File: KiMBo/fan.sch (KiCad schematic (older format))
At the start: 36 parts

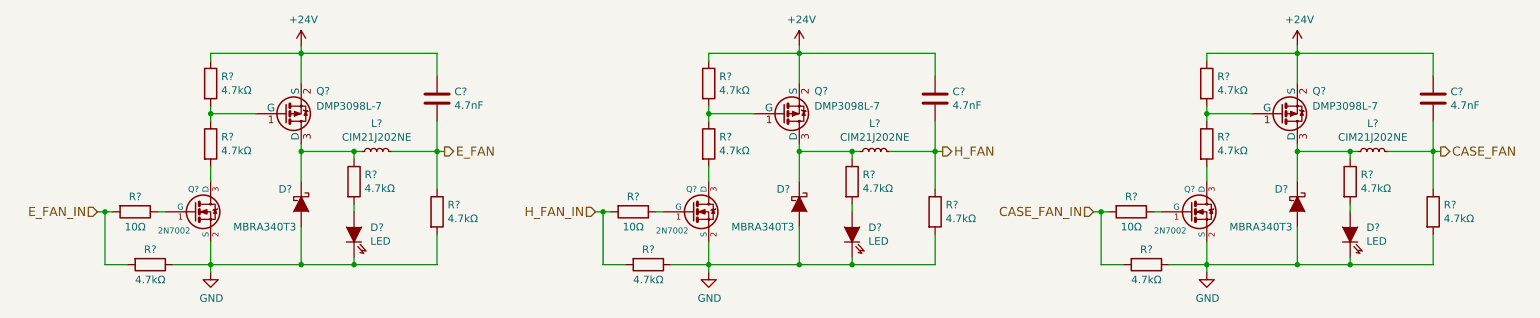
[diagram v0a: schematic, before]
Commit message: Update ferrite values, select fuse based on interrupt rating
The PSU needs to be able to supply at LEAST 25A to blow the fuse
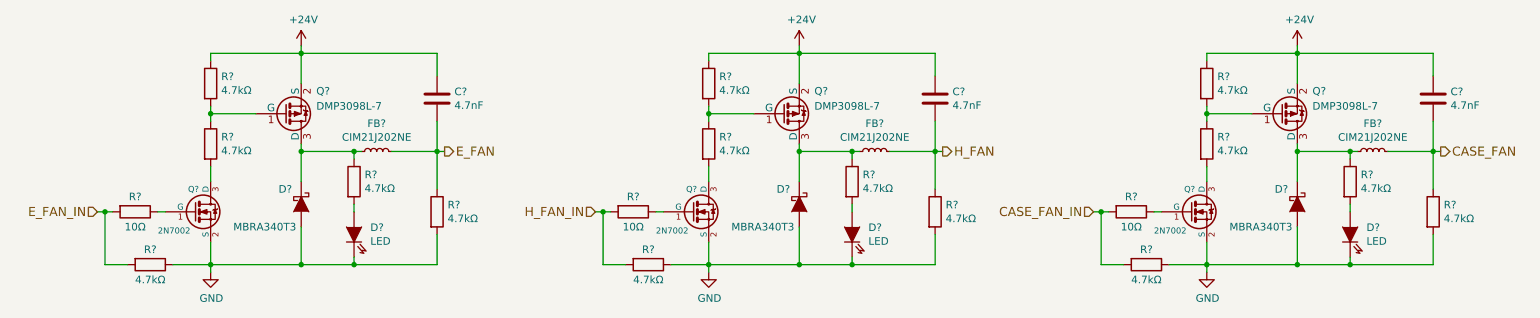
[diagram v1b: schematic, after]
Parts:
- gave numbers to parts that had none: 1
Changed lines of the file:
@@
 $EndComp
 $Comp
-L INDUCTOR_Small L?
+L INDUCTOR_Small FB?
 U 1 1 5B5F15E2
 P 5300 5200
-F 0 "L?" V 5485 5200 50  0000 C CNN
+F 0 "FB?" V 5485 5200 50  0000 C CNN
 F 1 "CIM21J202NE" V 5394 5200 50  0000 C CNN
 F 2 "" H 5300 5200 50  0000 C CNN
@@
 $EndComp
 $Comp
-L INDUCTOR_Small L?
+L INDUCTOR_Small FB?
 U 1 1 5B5F2422
 P 8600 5200
-F 0 "L?" V 8785 5200 50  0000 C CNN
+F 0 "FB?" V 8785 5200 50  0000 C CNN
 F 1 "CIM21J202NE" V 8694 5200 50  0000 C CNN
 F 2 "" H 8600 5200 50  0000 C CNN
@@
 $EndComp
 $Comp
-L INDUCTOR_Small L?
+L INDUCTOR_Small FB?
 U 1 1 5B5F2A0D
 P 11900 5200
-F 0 "L?" V 12085 5200 50  0000 C CNN
+F 0 "FB?" V 12085 5200 50  0000 C CNN
 F 1 "CIM21J202NE" V 11994 5200 50  0000 C CNN
 F 2 "" H 11900 5200 50  0000 C CNN

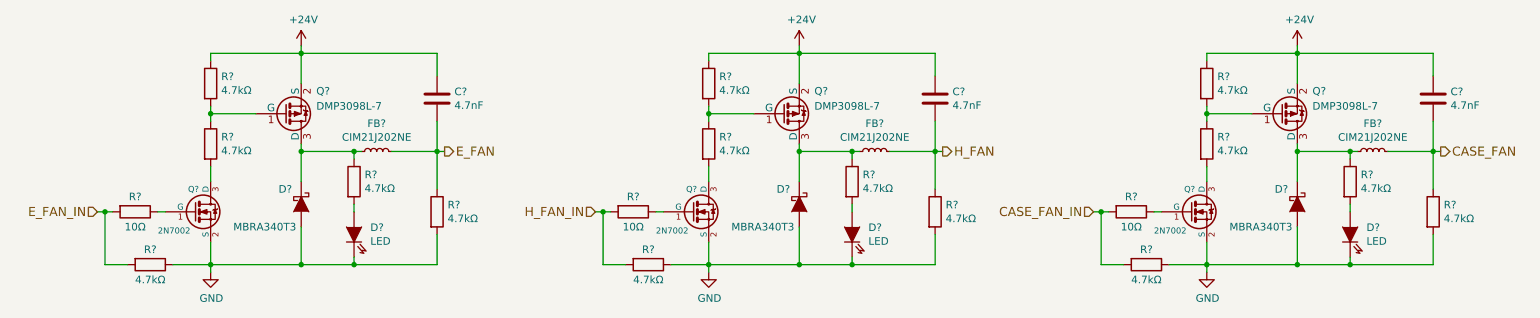
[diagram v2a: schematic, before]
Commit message: Annotate all components, now passing ERC, added ferrites to the rest of the connectors
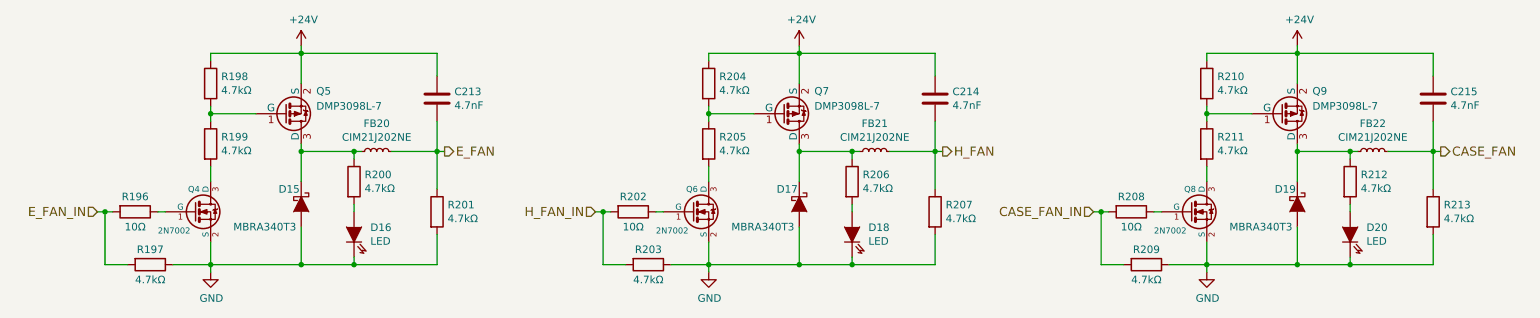
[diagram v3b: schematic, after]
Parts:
- gave numbers to parts that had none: 36
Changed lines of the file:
@@
 E_FAN
 $Comp
-L +24V #PWR0273
+L +24V #PWR0286
 U 1 1 5B5EFE55
 P 4800 4500
-F 0 "#PWR0273" H 4800 4350 50  0001 C CNN
+F 0 "#PWR0286" H 4800 4350 50  0001 C CNN
 F 1 "+24V" H 4815 4673 50  0000 C CNN
 F 2 "" H 4800 4500 50  0000 C CNN
@@
 $EndComp
 $Comp
-L GND #PWR0274
+L GND #PWR0287
 U 1 1 5B5EFE5B
 P 4200 6000
-F 0 "#PWR0274" H 4200 5750 50  0001 C CNN
+F 0 "#PWR0287" H 4200 5750 50  0001 C CNN
 F 1 "GND" H 4205 5827 50  0000 C CNN
 F 2 "" H 4200 6000 50  0000 C CNN
@@
 $EndComp
 $Comp
-L D_Schottky D?
+L D_Schottky D15
 U 1 1 5B5EFE61
 P 4800 5550
-F 0 "D?" V 4700 5400 50  0000 L CNN
+F 0 "D15" V 4700 5400 50  0000 L CNN
 F 1 "MBRA340T3" V 4950 5100 50  0000 L CNN
 F 2 "" H 4800 5550 50  0000 C CNN
@@
 $EndComp
 $Comp
-L R R?
+L R R196
 U 1 1 5B5EFE68
 P 3700 5600
-F 0 "R?" V 3600 5600 50  0000 C CNN
+F 0 "R196" V 3600 5600 50  0000 C CNN
 F 1 "10Ω" V 3800 5600 50  0000 C CNN
 F 2 "" V 3630 5600 50  0000 C CNN
@@
 $EndComp
 $Comp
-L 2N7002P,215 Q?
+L 2N7002P,215 Q4
 U 1 1 5B5EFE6F
 P 4100 5600
-F 0 "Q?" H 4050 5750 40  0000 L CNN
+F 0 "Q4" H 4050 5750 40  0000 L CNN
 F 1 "2N7002" H 3850 5475 40  0000 L CNN
 F 2 "SOT-23" H 3970 5702 29  0001 C CNN
@@
 $EndComp
 $Comp
-L LED_Short D?
+L LED_Short D16
 U 1 1 5B5EFE77
 P 5150 5750
-F 0 "D?" V 5196 5642 50  0000 R CNN
+F 0 "D16" V 5196 5642 50  0000 R CNN
 F 1 "LED" V 5105 5642 50  0000 R CNN
 F 2 "" H 5150 5750 50  0000 C CNN
@@
 $EndComp
 $Comp
-L R R?
+L R R200
 U 1 1 5B5EFE7E
 P 5150 5400
-F 0 "R?" H 5220 5446 50  0000 L CNN
+F 0 "R200" H 5220 5446 50  0000 L CNN
 F 1 "4.7kΩ" H 5220 5355 50  0000 L CNN
 F 2 "" V 5080 5400 50  0000 C CNN
@@
 $EndComp
 $Comp
-L R R?
+L R R198
 U 1 1 5B5EFE85
 P 4200 4750
-F 0 "R?" H 4270 4796 50  0000 L CNN
+F 0 "R198" H 4270 4796 50  0000 L CNN
 F 1 "4.7kΩ" H 4270 4705 50  0000 L CNN
 F 2 "" V 4130 4750 50  0000 C CNN
@@
 $EndComp
 $Comp
-L R R?
+L R R199
 U 1 1 5B5EFE8C
 P 4200 5150
-F 0 "R?" H 4270 5196 50  0000 L CNN
+F 0 "R199" H 4270 5196 50  0000 L CNN
 F 1 "4.7kΩ" H 4270 5105 50  0000 L CNN
 F 2 "" V 4130 5150 50  0000 C CNN
@@
 $EndComp
 $Comp
-L R R?
+L R R197
 U 1 1 5B5EFE93
 P 3800 5950
-F 0 "R?" V 3700 5950 50  0000 C CNN
+F 0 "R197" V 3700 5950 50  0000 C CNN
 F 1 "4.7kΩ" V 3900 5950 50  0000 C CNN
 F 2 "" V 3730 5950 50  0000 C CNN
@@
 $EndComp
 $Comp
-L R R?
+L R R201
 U 1 1 5B5EFE9A
 P 5700 5600
-F 0 "R?" H 5770 5646 50  0000 L CNN
+F 0 "R201" H 5770 5646 50  0000 L CNN
 F 1 "4.7kΩ" H 5770 5555 50  0000 L CNN
 F 2 "" V 5630 5600 50  0000 C CNN
@@
 $EndComp
 $Comp
-L C C?
+L C C213
 U 1 1 5B5EFEA1
 P 5700 4850
-F 0 "C?" H 5815 4896 50  0000 L CNN
+F 0 "C213" H 5815 4896 50  0000 L CNN
 F 1 "4.7nF" H 5815 4805 50  0000 L CNN
 F 2 "" H 5738 4700 50  0000 C CNN
@@
 	4200 4550 5700 4550
 $Comp
-L DMP3098L-7 Q?
+L DMP3098L-7 Q5
 U 1 1 5B5EFEC7
 P 4700 4950
-F 0 "Q?" H 4900 5100 50  0000 L CNN
+F 0 "Q5" H 4900 5100 50  0000 L CNN
 F 1 "DMP3098L-7" H 4900 5000 50  0000 L CNN
 F 2 "TO_SOT_Packages_SMD:SOT-23" H 4950 5025 50  0001 L CNN
@@
 $EndComp
 $Comp
-L INDUCTOR_Small FB?
+L INDUCTOR_Small FB20
 U 1 1 5B5F15E2
 P 5300 5200
-F 0 "FB?" V 5485 5200 50  0000 C CNN
+F 0 "FB20" V 5485 5200 50  0000 C CNN
 F 1 "CIM21J202NE" V 5394 5200 50  0000 C CNN
 F 2 "" H 5300 5200 50  0000 C CNN
@@
 H_FAN
 $Comp
-L +24V #PWR0275
+L +24V #PWR0288
 U 1 1 5B5F23AA
 P 8100 4500
-F 0 "#PWR0275" H 8100 4350 50  0001 C CNN
+F 0 "#PWR0288" H 8100 4350 50  0001 C CNN
 F 1 "+24V" H 8115 4673 50  0000 C CNN
 F 2 "" H 8100 4500 50  0000 C CNN
@@
 $EndComp
 $Comp
-L GND #PWR0276
+L GND #PWR0289
 U 1 1 5B5F23B0
 P 7500 6000
-F 0 "#PWR0276" H 7500 5750 50  0001 C CNN
+F 0 "#PWR0289" H 7500 5750 50  0001 C CNN
 F 1 "GND" H 7505 5827 50  0000 C CNN
 F 2 "" H 7500 6000 50  0000 C CNN
@@
 $EndComp
 $Comp
-L D_Schottky D?
+L D_Schottky D17
 U 1 1 5B5F23B6
 P 8100 5550
-F 0 "D?" V 8000 5400 50  0000 L CNN
+F 0 "D17" V 8000 5400 50  0000 L CNN
 F 1 "MBRA340T3" V 8250 5100 50  0000 L CNN
 F 2 "" H 8100 5550 50  0000 C CNN
@@
 $EndComp
 $Comp
-L R R?
+L R R202
 U 1 1 5B5F23BD
 P 7000 5600
-F 0 "R?" V 6900 5600 50  0000 C CNN
+F 0 "R202" V 6900 5600 50  0000 C CNN
 F 1 "10Ω" V 7100 5600 50  0000 C CNN
 F 2 "" V 6930 5600 50  0000 C CNN
@@
 $EndComp
 $Comp
-L LED_Short D?
+L LED_Short D18
 U 1 1 5B5F23CB
 P 8450 5750
-F 0 "D?" V 8496 5642 50  0000 R CNN
+F 0 "D18" V 8496 5642 50  0000 R CNN
 F 1 "LED" V 8405 5642 50  0000 R CNN
 F 2 "" H 8450 5750 50  0000 C CNN
@@
 $EndComp
 $Comp
-L R R?
+L R R206
 U 1 1 5B5F23D2
 P 8450 5400
-F 0 "R?" H 8520 5446 50  0000 L CNN
+F 0 "R206" H 8520 5446 50  0000 L CNN
 F 1 "4.7kΩ" H 8520 5355 50  0000 L CNN
 F 2 "" V 8380 5400 50  0000 C CNN
@@
 $EndComp
 $Comp
-L R R?
+L R R204
 U 1 1 5B5F23D9
 P 7500 4750
-F 0 "R?" H 7570 4796 50  0000 L CNN
+F 0 "R204" H 7570 4796 50  0000 L CNN
 F 1 "4.7kΩ" H 7570 4705 50  0000 L CNN
 F 2 "" V 7430 4750 50  0000 C CNN
@@
 $EndComp
 $Comp
-L R R?
+L R R205
 U 1 1 5B5F23E0
 P 7500 5150
-F 0 "R?" H 7570 5196 50  0000 L CNN
+F 0 "R205" H 7570 5196 50  0000 L CNN
 F 1 "4.7kΩ" H 7570 5105 50  0000 L CNN
 F 2 "" V 7430 5150 50  0000 C CNN
@@
 $EndComp
 $Comp
-L R R?
+L R R203
 U 1 1 5B5F23E7
 P 7100 5950
-F 0 "R?" V 7000 5950 50  0000 C CNN
+F 0 "R203" V 7000 5950 50  0000 C CNN
 F 1 "4.7kΩ" V 7200 5950 50  0000 C CNN
 F 2 "" V 7030 5950 50  0000 C CNN
@@
 $EndComp
 $Comp
-L R R?
+L R R207
 U 1 1 5B5F23EE
 P 9000 5600
-F 0 "R?" H 9070 5646 50  0000 L CNN
+F 0 "R207" H 9070 5646 50  0000 L CNN
 F 1 "4.7kΩ" H 9070 5555 50  0000 L CNN
 F 2 "" V 8930 5600 50  0000 C CNN
@@
 $EndComp
 $Comp
-L C C?
+L C C214
 U 1 1 5B5F23F5
 P 9000 4850
-F 0 "C?" H 9115 4896 50  0000 L CNN
+F 0 "C214" H 9115 4896 50  0000 L CNN
 F 1 "4.7nF" H 9115 4805 50  0000 L CNN
 F 2 "" H 9038 4700 50  0000 C CNN
@@
 	7500 4550 9000 4550
 $Comp
-L DMP3098L-7 Q?
+L DMP3098L-7 Q7
 U 1 1 5B5F241B
 P 8000 4950
-F 0 "Q?" H 8200 5100 50  0000 L CNN
+F 0 "Q7" H 8200 5100 50  0000 L CNN
 F 1 "DMP3098L-7" H 8200 5000 50  0000 L CNN
 F 2 "TO_SOT_Packages_SMD:SOT-23" H 8250 5025 50  0001 L CNN
@@
 $EndComp
 $Comp
-L INDUCTOR_Small FB?
+L INDUCTOR_Small FB21
 U 1 1 5B5F2422
 P 8600 5200
-F 0 "FB?" V 8785 5200 50  0000 C CNN
+F 0 "FB21" V 8785 5200 50  0000 C CNN
 F 1 "CIM21J202NE" V 8694 5200 50  0000 C CNN
 F 2 "" H 8600 5200 50  0000 C CNN
@@
 CASE_FAN
 $Comp
-L +24V #PWR0277
+L +24V #PWR0290
 U 1 1 5B5F2995
 P 11400 4500
-F 0 "#PWR0277" H 11400 4350 50  0001 C CNN
+F 0 "#PWR0290" H 11400 4350 50  0001 C CNN
 F 1 "+24V" H 11415 4673 50  0000 C CNN
 F 2 "" H 11400 4500 50  0000 C CNN
@@
 $EndComp
 $Comp
-L GND #PWR0278
+L GND #PWR0291
 U 1 1 5B5F299B
 P 10800 6000
-F 0 "#PWR0278" H 10800 5750 50  0001 C CNN
+F 0 "#PWR0291" H 10800 5750 50  0001 C CNN
 F 1 "GND" H 10805 5827 50  0000 C CNN
 F 2 "" H 10800 6000 50  0000 C CNN
@@
 $EndComp
 $Comp
-L D_Schottky D?
+L D_Schottky D19
 U 1 1 5B5F29A1
 P 11400 5550
-F 0 "D?" V 11300 5400 50  0000 L CNN
+F 0 "D19" V 11300 5400 50  0000 L CNN
 F 1 "MBRA340T3" V 11550 5100 50  0000 L CNN
 F 2 "" H 11400 5550 50  0000 C CNN
@@
 $EndComp
 $Comp
-L R R?
+L R R208
 U 1 1 5B5F29A8
 P 10300 5600
-F 0 "R?" V 10200 5600 50  0000 C CNN
+F 0 "R208" V 10200 5600 50  0000 C CNN
 F 1 "10Ω" V 10400 5600 50  0000 C CNN
 F 2 "" V 10230 5600 50  0000 C CNN
@@
 $EndComp
 $Comp
-L LED_Short D?
+L LED_Short D20
 U 1 1 5B5F29B6
 P 11750 5750
-F 0 "D?" V 11796 5642 50  0000 R CNN
+F 0 "D20" V 11796 5642 50  0000 R CNN
 F 1 "LED" V 11705 5642 50  0000 R CNN
 F 2 "" H 11750 5750 50  0000 C CNN
@@
 $EndComp
 $Comp
-L R R?
+L R R212
 U 1 1 5B5F29BD
 P 11750 5400
-F 0 "R?" H 11820 5446 50  0000 L CNN
+F 0 "R212" H 11820 5446 50  0000 L CNN
 F 1 "4.7kΩ" H 11820 5355 50  0000 L CNN
 F 2 "" V 11680 5400 50  0000 C CNN
@@
 $EndComp
 $Comp
-L R R?
+L R R210
 U 1 1 5B5F29C4
 P 10800 4750
-F 0 "R?" H 10870 4796 50  0000 L CNN
+F 0 "R210" H 10870 4796 50  0000 L CNN
 F 1 "4.7kΩ" H 10870 4705 50  0000 L CNN
 F 2 "" V 10730 4750 50  0000 C CNN
@@
 $EndComp
 $Comp
-L R R?
+L R R211
 U 1 1 5B5F29CB
 P 10800 5150
-F 0 "R?" H 10870 5196 50  0000 L CNN
+F 0 "R211" H 10870 5196 50  0000 L CNN
 F 1 "4.7kΩ" H 10870 5105 50  0000 L CNN
 F 2 "" V 10730 5150 50  0000 C CNN
@@
 $EndComp
 $Comp
-L R R?
+L R R209
 U 1 1 5B5F29D2
 P 10400 5950
-F 0 "R?" V 10300 5950 50  0000 C CNN
+F 0 "R209" V 10300 5950 50  0000 C CNN
 F 1 "4.7kΩ" V 10500 5950 50  0000 C CNN
 F 2 "" V 10330 5950 50  0000 C CNN
@@
 $EndComp
 $Comp
-L R R?
+L R R213
 U 1 1 5B5F29D9
 P 12300 5600
-F 0 "R?" H 12370 5646 50  0000 L CNN
+F 0 "R213" H 12370 5646 50  0000 L CNN
 F 1 "4.7kΩ" H 12370 5555 50  0000 L CNN
 F 2 "" V 12230 5600 50  0000 C CNN
@@
 $EndComp
 $Comp
-L C C?
+L C C215
 U 1 1 5B5F29E0
 P 12300 4850
-F 0 "C?" H 12415 4896 50  0000 L CNN
+F 0 "C215" H 12415 4896 50  0000 L CNN
 F 1 "4.7nF" H 12415 4805 50  0000 L CNN
 F 2 "" H 12338 4700 50  0000 C CNN
@@
 	10800 4550 12300 4550
 $Comp
-L DMP3098L-7 Q?
+L DMP3098L-7 Q9
 U 1 1 5B5F2A06
 P 11300 4950
-F 0 "Q?" H 11500 5100 50  0000 L CNN
+F 0 "Q9" H 11500 5100 50  0000 L CNN
 F 1 "DMP3098L-7" H 11500 5000 50  0000 L CNN
 F 2 "TO_SOT_Packages_SMD:SOT-23" H 11550 5025 50  0001 L CNN
@@
 $EndComp
 $Comp
-L INDUCTOR_Small FB?
+L INDUCTOR_Small FB22
 U 1 1 5B5F2A0D
 P 11900 5200
-F 0 "FB?" V 12085 5200 50  0000 C CNN
+F 0 "FB22" V 12085 5200 50  0000 C CNN
 F 1 "CIM21J202NE" V 11994 5200 50  0000 C CNN
 F 2 "" H 11900 5200 50  0000 C CNN
@@
 $EndComp
 $Comp
-L 2N7002P,215 Q?
+L 2N7002P,215 Q6
 U 1 1 5B5FA7B8
 P 7400 5600
-F 0 "Q?" H 7350 5750 40  0000 L CNN
+F 0 "Q6" H 7350 5750 40  0000 L CNN
 F 1 "2N7002" H 7150 5475 40  0000 L CNN
 F 2 "SOT-23" H 7270 5702 29  0001 C CNN
@@
 $EndComp
 $Comp
-L 2N7002P,215 Q?
+L 2N7002P,215 Q8
 U 1 1 5B5FA86F
 P 10700 5600
-F 0 "Q?" H 10650 5750 40  0000 L CNN
+F 0 "Q8" H 10650 5750 40  0000 L CNN
 F 1 "2N7002" H 10450 5475 40  0000 L CNN
 F 2 "SOT-23" H 10570 5702 29  0001 C CNN
